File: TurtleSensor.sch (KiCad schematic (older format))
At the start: 13 parts, among them IC1 ATMEGA328-P, J1 ISPConnector, J2 FTDIConnector, U1 HTU21DBreakout, U2 W25Q32FlashBreakout

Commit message: mostly routed
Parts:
- removed IC1: ATMEGA328-P, Housings_DIP:DIP-28_W7.62mm, symbol ATMEGA328-P
- removed U1: HTU21DBreakout, Socket_Strips:Socket_Strip_Straight_1x04, symbol HTU21DBreakout
- removed U2: W25Q32FlashBreakout, Socket_Strips:Socket_Strip_Straight_1x06, symbol W25Q32FlashBreakout
- added IC1: ATMEGA328P-A, Housings_QFP:TQFP-32_7x7mm_Pitch0.8mm, symbol ATMEGA328P-A
- added U1: SI7021, SI7021:DFN-6%2f3MM, symbol SI7021
- added U2: W25Q32FVSSIG, W25Q32FVSSIG:SOIC127P790X216-8N, symbol W25Q32FVSSIG
- 22pF1, 22pF2, C2: footprint Capacitors_ThroughHole:C_Disc_D3_P2.5 -> Capacitors_SMD:C_0805_HandSoldering
- 8MHz1: footprint Crystals:Crystal_HC49-U_Vertical -> Crystals:Crystal_HC49-SD_SMD
- C1: value 25µF -> 10µF; footprint Capacitors_ThroughHole:C_Radial_D5_L11_P2.5 -> Capacitors_SMD:C_0805_HandSoldering
- D1: footprint LEDs:LED-5MM -> LEDs:LED_0805
- R1: footprint Resistors_ThroughHole:Resistor_Horizontal_RM10mm -> Resistors_SMD:R_0805_HandSoldering
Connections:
- wire segments 63 -> 67
- no-connect marks 12 -> 14
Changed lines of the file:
@@
 LIBS:contrib
 LIBS:valves
+LIBS:SI7021
+LIBS:W25Q32FVSSIG
 LIBS:TurtleSensor-cache
 EELAYER 25 0
@@
 P 2150 2600
 F 0 "C1" H 2175 2700 50  0000 L CNN
-F 1 "25µF" H 2175 2500 50  0000 L CNN
-F 2 "Capacitors_ThroughHole:C_Radial_D5_L11_P2.5" H 2188 2450 30  0001 C CNN
+F 1 "10µF" H 2175 2500 50  0000 L CNN
+F 2 "Capacitors_SMD:C_0805_HandSoldering" H 2188 2450 30  0001 C CNN
 F 3 "" H 2150 2600 60  0000 C CNN
 	1    2150 2600
@@
 F 0 "D1" H 4900 1750 50  0000 C CNN
 F 1 "LED" H 4900 1550 50  0000 C CNN
-F 2 "LEDs:LED-5MM" H 4900 1650 60  0001 C CNN
+F 2 "LEDs:LED_0805" H 4900 1650 60  0001 C CNN
 F 3 "" H 4900 1650 60  0000 C CNN
 	1    4900 1650
@@
 F 0 "R1" V 5430 1650 50  0000 C CNN
 F 1 "470" V 5350 1650 50  0000 C CNN
-F 2 "Resistors_ThroughHole:Resistor_Horizontal_RM10mm" V 5280 1650 30  0001 C CNN
+F 2 "Resistors_SMD:R_0805_HandSoldering" V 5280 1650 30  0001 C CNN
 F 3 "" H 5350 1650 30  0000 C CNN
 	1    5350 1650
@@
 F 0 "8MHz1" H 5200 2350 50  0000 C CNN
 F 1 "Crystal" H 5200 2050 50  0000 C CNN
-F 2 "Crystals:Crystal_HC49-U_Vertical" H 5200 2200 50  0001 C CNN
+F 2 "Crystals:Crystal_HC49-SD_SMD" H 5200 2200 50  0001 C CNN
 F 3 "" H 5200 2200 50  0000 C CNN
 	1    5200 2200
@@
 F 0 "22pF1" H 5675 2150 50  0000 L CNN
 F 1 "C" H 5675 1950 50  0000 L CNN
-F 2 "Capacitors_ThroughHole:C_Disc_D3_P2.5" H 5688 1900 50  0001 C CNN
+F 2 "Capacitors_SMD:C_0805_HandSoldering" H 5688 1900 50  0001 C CNN
 F 3 "" H 5650 2050 50  0000 C CNN
 	1    5650 2050
@@
 F 0 "22pF2" H 5675 2450 50  0000 L CNN
 F 1 "C" H 5675 2250 50  0000 L CNN
-F 2 "Capacitors_ThroughHole:C_Disc_D3_P2.5" H 5688 2200 50  0001 C CNN
+F 2 "Capacitors_SMD:C_0805_HandSoldering" H 5688 2200 50  0001 C CNN
 F 3 "" H 5650 2350 50  0000 C CNN
 	1    5650 2350
@@
 	4300 2250 4800 2250
 Connection ~ 5200 2350
-$Comp
-L HTU21DBreakout U1
-U 1 1 56C0C860
-P 6850 2550
-F 0 "U1" H 6850 2400 60  0000 C CNN
-F 1 "HTU21DBreakout" H 6850 3000 60  0000 C CNN
-F 2 "Socket_Strips:Socket_Strip_Straight_1x04" H 6750 2600 60  0001 C CNN
-F 3 "" H 6750 2600 60  0000 C CNN
-	1    6850 2550
-	1    0    0    -1
-$EndComp
-Wire Wire Line
-	6400 2350 6350 2350
-Wire Wire Line
-	6350 2350 6350 2700
-Wire Wire Line
-	6400 2250 6350 2250
+Wire Wire Line
+	6350 2250 6450 2250
 Wire Wire Line
 	6350 2250 6350 2050
@@
 $EndComp
 $Comp
-L W25Q32FlashBreakout U2
-U 1 1 56C0D583
-P 6900 3600
-F 0 "U2" H 6900 3250 60  0000 C CNN
-F 1 "W25Q32FlashBreakout" H 6900 4050 60  0000 C CNN
-F 2 "Socket_Strips:Socket_Strip_Straight_1x06" H 6750 3600 60  0001 C CNN
-F 3 "" H 6750 3600 60  0000 C CNN
-	1    6900 3600
-	1    0    0    -1
-$EndComp
-$Comp
 L +BATT #PWR05
 U 1 1 56C0D5FA
-P 6300 3150
-F 0 "#PWR05" H 6300 3000 50  0001 C CNN
-F 1 "+BATT" H 6300 3290 50  0000 C CNN
-F 2 "" H 6300 3150 50  0000 C CNN
-F 3 "" H 6300 3150 50  0000 C CNN
-	1    6300 3150
+P 8250 3150
+F 0 "#PWR05" H 8250 3000 50  0001 C CNN
+F 1 "+BATT" H 8250 3290 50  0000 C CNN
+F 2 "" H 8250 3150 50  0000 C CNN
+F 3 "" H 8250 3150 50  0000 C CNN
+	1    8250 3150
 	1    0    0    -1
 $EndComp
@@
 L GND #PWR06
 U 1 1 56C0D622
-P 6300 3900
-F 0 "#PWR06" H 6300 3650 50  0001 C CNN
-F 1 "GND" H 6300 3750 50  0000 C CNN
-F 2 "" H 6300 3900 50  0000 C CNN
-F 3 "" H 6300 3900 50  0000 C CNN
-	1    6300 3900
-	1    0    0    -1
-$EndComp
-Wire Wire Line
-	6500 3800 6300 3800
-Wire Wire Line
-	6300 3800 6300 3900
-Wire Wire Line
-	6500 3300 6300 3300
-Wire Wire Line
-	6300 3300 6300 3150
-Text Label 6300 3400 0    60   ~ 0
+P 8250 3900
+F 0 "#PWR06" H 8250 3650 50  0001 C CNN
+F 1 "GND" H 8250 3750 50  0000 C CNN
+F 2 "" H 8250 3900 50  0000 C CNN
+F 3 "" H 8250 3900 50  0000 C CNN
+	1    8250 3900
+	1    0    0    -1
+$EndComp
+Text Label 6550 3250 0    60   ~ 0
 ~CS
-Text Label 6300 3600 0    60   ~ 0
+Text Label 6500 3650 0    60   ~ 0
 MOSI
-Text Label 6300 3500 0    60   ~ 0
+Text Label 6500 3750 0    60   ~ 0
 MISO
-Text Label 6300 3700 0    60   ~ 0
+Text Label 6550 3350 0    60   ~ 0
 SCK
-Wire Wire Line
-	6500 3400 6300 3400
-Wire Wire Line
-	6300 3500 6500 3500
-Wire Wire Line
-	6300 3600 6500 3600
-Wire Wire Line
-	6500 3700 6300 3700
-Wire Wire Line
-	6150 2450 6400 2450
-Wire Wire Line
-	6150 2550 6400 2550
-Text Label 6150 2450 0    60   ~ 0
+Text Label 7400 2250 0    60   ~ 0
 SDA
-Text Label 6150 2550 0    60   ~ 0
+Text Label 7400 2450 0    60   ~ 0
 SCL
 Text Label 4550 1850 0    60   ~ 0
@@
 Wire Wire Line
 	4300 2900 4500 2900
-$Comp
-L ATMEGA328-P IC1
-U 1 1 56C6AD4C
-P 3300 2650
-F 0 "IC1" H 2550 3900 50  0000 L BNN
-F 1 "ATMEGA328-P" H 3700 1250 50  0000 L BNN
-F 2 "Housings_DIP:DIP-28_W7.62mm" H 3300 2650 50  0001 C CIN
-F 3 "" H 3300 2650 50  0000 C CNN
-	1    3300 2650
-	1    0    0    -1
-$EndComp
-Wire Wire Line
-	1100 3650 2150 3650
+Wire Wire Line
+	1100 3650 2400 3650
 Connection ~ 2150 3650
 Wire Wire Line
@@
 F 0 "C2" H 4275 6500 50  0000 L CNN
 F 1 "0.1uF" H 4275 6300 50  0000 L CNN
-F 2 "Capacitors_ThroughHole:C_Disc_D3_P2.5" H 4288 6250 50  0001 C CNN
+F 2 "Capacitors_SMD:C_0805_HandSoldering" H 4288 6250 50  0001 C CNN
 F 3 "" H 4250 6400 50  0000 C CNN
 	1    4250 6400
@@
 Wire Wire Line
 	4100 6400 3700 6400
+$Comp
+L SI7021 U1
+U 1 1 56EDF09F
+P 6850 2350
+F 0 "U1" H 6550 2570 50  0000 L CNN
+F 1 "SI7021" H 6550 2060 50  0000 L CNN
+F 2 "SI7021:DFN-6%2f3MM" H 6850 2350 50  0001 L CNN
+F 3 "" H 6850 2350 60  0000 C CNN
+	1    6850 2350
+	1    0    0    -1
+$EndComp
+Wire Wire Line
+	6450 2450 6350 2450
+Wire Wire Line
+	6350 2450 6350 2700
+Wire Wire Line
+	7250 2450 7400 2450
+Wire Wire Line
+	7400 2250 7250 2250
+$Comp
+L W25Q32FVSSIG U2
+U 1 1 56EDF390
+P 7450 3550
+F 0 "U2" H 6960 3980 50  0000 L CNN
+F 1 "W25Q32FVSSIG" H 6960 3070 50  0000 L CNN
+F 2 "W25Q32FVSSIG:SOIC127P790X216-8N" H 7450 3550 50  0001 L CNN
+F 3 "" H 7450 3550 60  0000 C CNN
+	1    7450 3550
+	1    0    0    -1
+$EndComp
+Wire Wire Line
+	8250 3900 8250 3850
+Wire Wire Line
+	8250 3850 8150 3850
+Wire Wire Line
+	8150 3250 8250 3250
+Wire Wire Line
+	8250 3250 8250 3150
+Wire Wire Line
+	6750 3250 6550 3250
+Wire Wire Line
+	6550 3350 6750 3350
+Wire Wire Line
+	6750 3650 6500 3650
+Wire Wire Line
+	6500 3750 6750 3750
+$Comp
+L +BATT #PWR013
+U 1 1 56EDFB62
+P 6300 3150
+F 0 "#PWR013" H 6300 3000 50  0001 C CNN
+F 1 "+BATT" H 6300 3290 50  0000 C CNN
+F 2 "" H 6300 3150 50  0000 C CNN
+F 3 "" H 6300 3150 50  0000 C CNN
+	1    6300 3150
+	1    0    0    -1
+$EndComp
+Wire Wire Line
+	6300 3150 6300 3850
+Wire Wire Line
+	6300 3850 6750 3850
+Wire Wire Line
+	6750 3550 6300 3550
+Connection ~ 6300 3550
+$Comp
+L ATMEGA328P-A IC1
+U 1 1 56EE0075
+P 3300 2650
+F 0 "IC1" H 2550 3900 50  0000 L BNN
+F 1 "ATMEGA328P-A" H 3700 1250 50  0000 L BNN
+F 2 "Housings_QFP:TQFP-32_7x7mm_Pitch0.8mm" H 3300 2650 50  0000 C CIN
+F 3 "" H 3300 2650 50  0000 C CNN
+	1    3300 2650
+	1    0    0    -1
+$EndComp
+Wire Wire Line
+	2400 1650 2150 1650
+Connection ~ 2150 1650
+NoConn ~ 2400 2900
+NoConn ~ 2400 3000
 $EndSCHEMATC

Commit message: switching to new components
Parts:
- J2: footprint Socket_Strips:Socket_Strip_Angled_1x06 -> Pin_Headers:Pin_Header_Straight_1x06
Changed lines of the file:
@@
 F 0 "J2" H 5300 6600 60  0000 C CNN
 F 1 "FTDIConnector" H 5350 5350 60  0000 C CNN
-F 2 "Socket_Strips:Socket_Strip_Angled_1x06" H 5550 5650 60  0001 C CNN
+F 2 "Pin_Headers:Pin_Header_Straight_1x06" H 5550 5650 60  0001 C CNN
 F 3 "" H 5550 5650 60  0000 C CNN
 	1    5550 6000

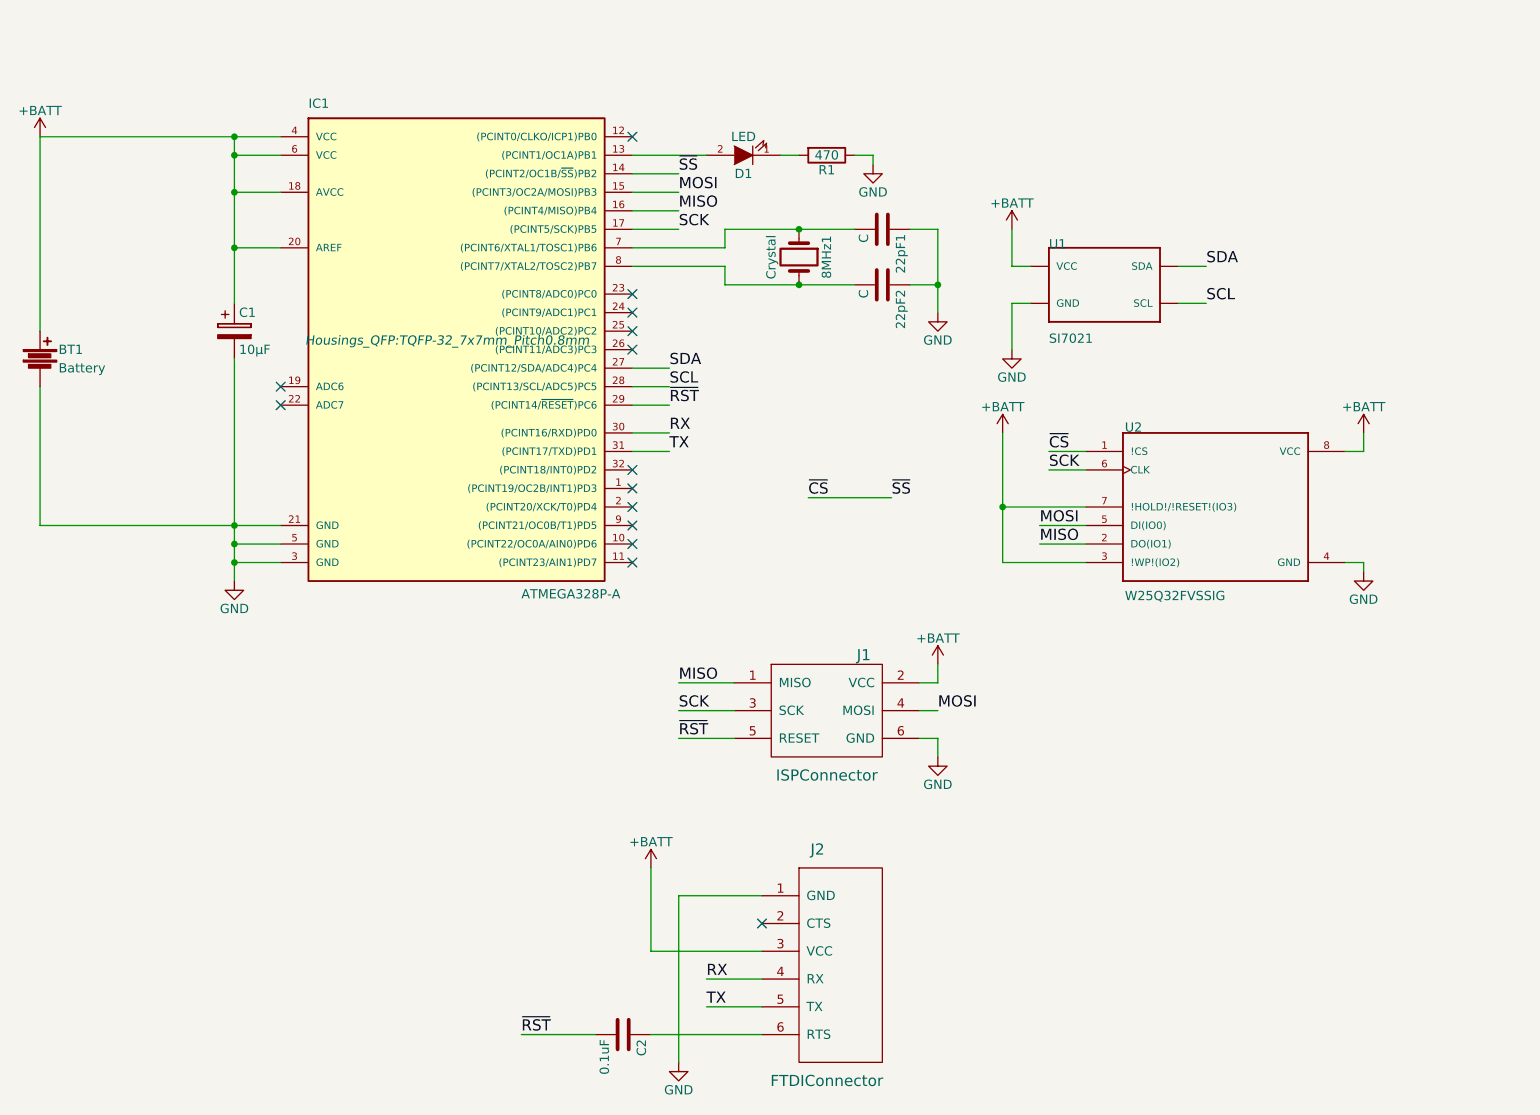
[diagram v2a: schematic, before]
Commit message: added missing pullups and lots
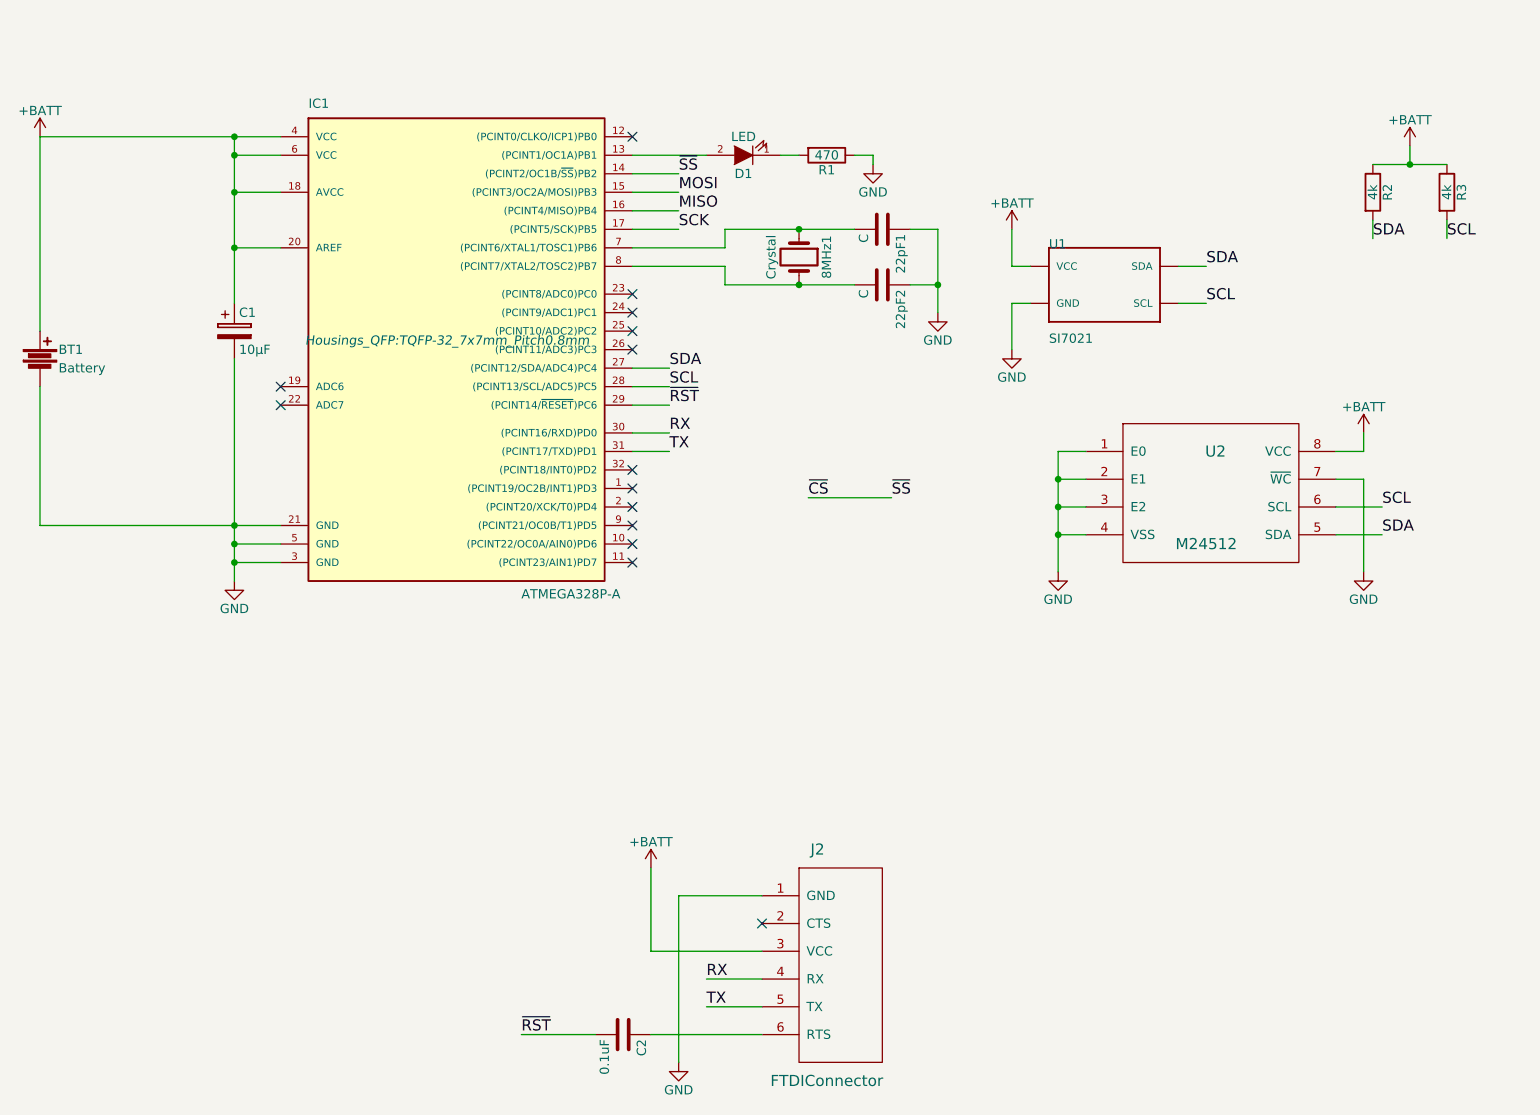
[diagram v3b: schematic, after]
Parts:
- removed J1: ISPConnector, Socket_Strips:Socket_Strip_Straight_2x03, symbol ISPConnector
- removed U2: W25Q32FVSSIG, W25Q32FVSSIG:SOIC127P790X216-8N, symbol W25Q32FVSSIG
- added R2, R3: 4k, Resistors_SMD:R_0805_HandSoldering, symbol R
- added U2: M24512, SMD_Packages:SOIC-8-N, symbol M24512
- 8MHz1: footprint Crystals:Crystal_HC49-SD_SMD -> footprints:2-SMD
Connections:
- net +BATT: now also R2.1, R3.1, U2.8 (VCC)
- net GND: now also U2.1 (E0), U2.2 (E1), U2.3 (E2), U2.4 (VSS), U2.7 (~WC)
- net SCL: now also R3.2, U2.6 (SCL)
- net SDA: now also R2.2, U2.5 (SDA)
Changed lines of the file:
@@
 F 0 "8MHz1" H 5200 2350 50  0000 C CNN
 F 1 "Crystal" H 5200 2050 50  0000 C CNN
-F 2 "Crystals:Crystal_HC49-SD_SMD" H 5200 2200 50  0001 C CNN
+F 2 "footprints:2-SMD" H 5200 2200 50  0001 C CNN
 F 3 "" H 5200 2200 50  0000 C CNN
 	1    5200 2200
@@
 	1    0    0    -1
 $EndComp
-Text Label 6550 3250 0    60   ~ 0
-~CS
-Text Label 6500 3650 0    60   ~ 0
-MOSI
-Text Label 6500 3750 0    60   ~ 0
-MISO
-Text Label 6550 3350 0    60   ~ 0
-SCK
 Text Label 7400 2250 0    60   ~ 0
 SDA
@@
 	1    0    0    -1
 $EndComp
-$Comp
-L ISPConnector J1
-U 1 1 56C74919
-P 5350 4650
-F 0 "J1" H 5550 4950 60  0000 C CNN
-F 1 "ISPConnector" H 5350 4300 60  0000 C CNN
-F 2 "Socket_Strips:Socket_Strip_Straight_2x03" H 5100 4550 60  0001 C CNN
-F 3 "" H 5100 4550 60  0000 C CNN
-	1    5350 4650
-	1    0    0    -1
-$EndComp
-$Comp
-L GND #PWR09
-U 1 1 56C74A3C
-P 5950 4900
-F 0 "#PWR09" H 5950 4650 50  0001 C CNN
-F 1 "GND" H 5950 4750 50  0000 C CNN
-F 2 "" H 5950 4900 50  0000 C CNN
-F 3 "" H 5950 4900 50  0000 C CNN
-	1    5950 4900
-	1    0    0    -1
-$EndComp
-Wire Wire Line
-	5950 4900 5950 4800
-Wire Wire Line
-	5950 4800 5850 4800
-$Comp
-L +BATT #PWR010
-U 1 1 56C74AB3
-P 5950 4400
-F 0 "#PWR010" H 5950 4250 50  0001 C CNN
-F 1 "+BATT" H 5950 4540 50  0000 C CNN
-F 2 "" H 5950 4400 50  0000 C CNN
-F 3 "" H 5950 4400 50  0000 C CNN
-	1    5950 4400
-	1    0    0    -1
-$EndComp
-Wire Wire Line
-	5950 4400 5950 4500
-Wire Wire Line
-	5950 4500 5850 4500
-Wire Wire Line
-	5850 4650 5950 4650
-Text Label 5950 4650 0    60   ~ 0
-MOSI
-Text Label 4550 4650 0    60   ~ 0
-SCK
-Text Label 4550 4500 0    60   ~ 0
-MISO
-Text Label 4550 4800 0    60   ~ 0
-~RST
-Wire Wire Line
-	4550 4500 4850 4500
-Wire Wire Line
-	4850 4650 4550 4650
-Wire Wire Line
-	4550 4800 4850 4800
 Wire Wire Line
 	4300 3000 4500 3000
@@
 RX
 $Comp
-L GND #PWR011
+L GND #PWR09
 U 1 1 56DB7AC0
 P 4550 6550
-F 0 "#PWR011" H 4550 6300 50  0001 C CNN
+F 0 "#PWR09" H 4550 6300 50  0001 C CNN
 F 1 "GND" H 4550 6400 50  0000 C CNN
 F 2 "" H 4550 6550 50  0000 C CNN
@@
 $EndComp
 $Comp
-L +BATT #PWR012
+L +BATT #PWR010
 U 1 1 56DB7B9E
 P 4400 5500
-F 0 "#PWR012" H 4400 5350 50  0001 C CNN
+F 0 "#PWR010" H 4400 5350 50  0001 C CNN
 F 1 "+BATT" H 4400 5640 50  0000 C CNN
 F 2 "" H 4400 5500 50  0000 C CNN
@@
 Wire Wire Line
 	7400 2250 7250 2250
-$Comp
-L W25Q32FVSSIG U2
-U 1 1 56EDF390
-P 7450 3550
-F 0 "U2" H 6960 3980 50  0000 L CNN
-F 1 "W25Q32FVSSIG" H 6960 3070 50  0000 L CNN
-F 2 "W25Q32FVSSIG:SOIC127P790X216-8N" H 7450 3550 50  0001 L CNN
-F 3 "" H 7450 3550 60  0000 C CNN
-	1    7450 3550
-	1    0    0    -1
-$EndComp
-Wire Wire Line
-	8250 3900 8250 3850
-Wire Wire Line
-	8250 3850 8150 3850
-Wire Wire Line
-	8150 3250 8250 3250
+Wire Wire Line
+	8250 3400 8250 3900
 Wire Wire Line
 	8250 3250 8250 3150
-Wire Wire Line
-	6750 3250 6550 3250
-Wire Wire Line
-	6550 3350 6750 3350
-Wire Wire Line
-	6750 3650 6500 3650
-Wire Wire Line
-	6500 3750 6750 3750
-$Comp
-L +BATT #PWR013
-U 1 1 56EDFB62
-P 6300 3150
-F 0 "#PWR013" H 6300 3000 50  0001 C CNN
-F 1 "+BATT" H 6300 3290 50  0000 C CNN
-F 2 "" H 6300 3150 50  0000 C CNN
-F 3 "" H 6300 3150 50  0000 C CNN
-	1    6300 3150
-	1    0    0    -1
-$EndComp
-Wire Wire Line
-	6300 3150 6300 3850
-Wire Wire Line
-	6300 3850 6750 3850
-Wire Wire Line
-	6750 3550 6300 3550
-Connection ~ 6300 3550
 $Comp
 L ATMEGA328P-A IC1
@@
 NoConn ~ 2400 2900
 NoConn ~ 2400 3000
+$Comp
+L M24512 U2
+U 1 1 575F3396
+P 7400 3600
+F 0 "U2" H 7450 3950 60  0000 C CNN
+F 1 "M24512" H 7400 3450 60  0000 C CNN
+F 2 "SMD_Packages:SOIC-8-N" H 7400 3600 60  0001 C CNN
+F 3 "" H 7400 3600 60  0000 C CNN
+	1    7400 3600
+	1    0    0    -1
+$EndComp
+Wire Wire Line
+	8250 3250 8100 3250
+Wire Wire Line
+	8100 3400 8250 3400
+Wire Wire Line
+	6750 3250 6600 3250
+Wire Wire Line
+	6600 3250 6600 3900
+Wire Wire Line
+	6600 3700 6750 3700
+Wire Wire Line
+	6750 3550 6600 3550
+Connection ~ 6600 3550
+Wire Wire Line
+	6600 3400 6750 3400
+Connection ~ 6600 3400
+$Comp
+L GND #PWR011
+U 1 1 575F35E6
+P 6600 3900
+F 0 "#PWR011" H 6600 3650 50  0001 C CNN
+F 1 "GND" H 6600 3750 50  0000 C CNN
+F 2 "" H 6600 3900 50  0000 C CNN
+F 3 "" H 6600 3900 50  0000 C CNN
+	1    6600 3900
+	1    0    0    -1
+$EndComp
+Connection ~ 6600 3700
+Wire Wire Line
+	8100 3550 8350 3550
+Wire Wire Line
+	8350 3700 8100 3700
+Text Label 8350 3550 0    60   ~ 0
+SCL
+Text Label 8350 3700 0    60   ~ 0
+SDA
+$Comp
+L +BATT #PWR012
+U 1 1 5768BC03
+P 8500 1600
+F 0 "#PWR012" H 8500 1450 50  0001 C CNN
+F 1 "+BATT" H 8500 1740 50  0000 C CNN
+F 2 "" H 8500 1600 50  0000 C CNN
+F 3 "" H 8500 1600 50  0000 C CNN
+	1    8500 1600
+	1    0    0    -1
+$EndComp
+$Comp
+L R R2
+U 1 1 5768BC8F
+P 8300 1850
+F 0 "R2" V 8380 1850 50  0000 C CNN
+F 1 "4k" V 8300 1850 50  0000 C CNN
+F 2 "Resistors_SMD:R_0805_HandSoldering" V 8230 1850 50  0001 C CNN
+F 3 "" H 8300 1850 50  0000 C CNN
+	1    8300 1850
+	1    0    0    -1
+$EndComp
+$Comp
+L R R3
+U 1 1 5768BDF6
+P 8700 1850
+F 0 "R3" V 8780 1850 50  0000 C CNN
+F 1 "4k" V 8700 1850 50  0000 C CNN
+F 2 "Resistors_SMD:R_0805_HandSoldering" V 8630 1850 50  0001 C CNN
+F 3 "" H 8700 1850 50  0000 C CNN
+	1    8700 1850
+	1    0    0    -1
+$EndComp
+Wire Wire Line
+	8300 1700 8700 1700
+Wire Wire Line
+	8500 1600 8500 1700
+Connection ~ 8500 1700
+Text Label 8300 2100 0    60   ~ 0
+SDA
+Text Label 8700 2100 0    60   ~ 0
+SCL
+Wire Wire Line
+	8700 2000 8700 2100
+Wire Wire Line
+	8300 2000 8300 2100
 $EndSCHEMATC

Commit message: sent board to be manufactured
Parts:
- BT1: footprint Socket_Strips:Socket_Strip_Straight_1x02 -> footprints:2477Holder
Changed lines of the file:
@@
 F 0 "BT1" H 1200 2800 50  0000 L CNN
 F 1 "Battery" H 1200 2700 50  0000 L CNN
-F 2 "Socket_Strips:Socket_Strip_Straight_1x02" V 1100 2790 60  0001 C CNN
+F 2 "footprints:2477Holder" V 1100 2790 60  0001 C CNN
 F 3 "" V 1100 2790 60  0000 C CNN
 	1    1100 2750

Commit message: fixed programming resistor, pcb is now circular v4
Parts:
- added 2k: R, symbol R
- renumbered 8MHz1 to 32KHz1
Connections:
- net +BATT: now also 2k.1
- net ~RST: now also 2k.2
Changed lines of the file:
@@
 	4700 1650 4300 1650
 $Comp
-L Crystal 8MHz1
+L Crystal 32KHz1
 U 1 1 56B6E109
 P 5200 2200
-F 0 "8MHz1" H 5200 2350 50  0000 C CNN
+F 0 "32KHz1" H 5200 2350 50  0000 C CNN
 F 1 "Crystal" H 5200 2050 50  0000 C CNN
 F 2 "footprints:2-SMD" H 5200 2200 50  0001 C CNN
@@
 TX
 Wire Wire Line
-	4400 5950 5000 5950
+	3950 5950 5000 5950
 Wire Wire Line
 	4550 6550 4550 5650
@@
 Wire Wire Line
 	8300 2000 8300 2100
+$Comp
+L R 2k
+U 1 1 57C323B4
+P 3950 6150
+F 0 "2k" V 4030 6150 50  0000 C CNN
+F 1 "R" V 3950 6150 50  0000 C CNN
+F 2 "" V 3880 6150 50  0000 C CNN
+F 3 "" H 3950 6150 50  0000 C CNN
+	1    3950 6150
+	1    0    0    -1
+$EndComp
+Connection ~ 4400 5950
+Wire Wire Line
+	3950 5950 3950 6000
+Wire Wire Line
+	3950 6300 3950 6400
+Connection ~ 3950 6400
 $EndSCHEMATC
